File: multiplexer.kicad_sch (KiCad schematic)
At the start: 0 parts

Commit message: FINISH SCHEMATICS
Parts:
- added C6: 10uf, symbol Device:C
- added JP10, JP2, JP3, JP4, JP5: SolderJumper_2_Open, symbol Jumper:SolderJumper_2_Open
- added R10, R11, R12, R13, R14, R19: 10k, symbol Device:R
- added U2: TCA9548APWR, Package_SO:TSSOP-24_4.4x7.8mm_P0.65mm, symbol Interface_Expansion:TCA9548APWR
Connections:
- new net: JP10.2 (B), R10.2
- new net: JP5.2 (B), R14.2, U2.1 (A0)
- new net: JP4.2 (B), R13.2, U2.2 (A1)
- new net: JP2.2 (B), R19.2
- new net: JP3.1 (A), R12.2, U2.21 (A2)
- new net: R11.2, U2.3 (~{RESET})
- new net GND: C6.2, R12.1, R13.1, R14.1, U2.12 (GND)
- new net SC0: U2.5 (SC0)
- new net SC1: U2.7 (SC1)
- new net SC2: U2.9 (SC2)
- new net SC3: U2.11 (SC3)
- new net SC4: U2.14 (SC4)
- new net SC5: U2.16 (SC5)
- new net SC6: U2.18 (SC6)
- new net SC7: U2.20 (SC7)
- new net SCL_IN: JP10.1 (A), U2.22 (SCL)
- new net SD0: U2.4 (SD0)
- new net SD1: U2.6 (SD1)
- new net SD2: U2.8 (SD2)
- new net SD3: U2.10 (SD3)
- new net SD4: U2.13 (SD4)
- new net SD5: U2.15 (SD5)
- new net SD6: U2.17 (SD6)
- new net SD7: U2.19 (SD7)
- new net SDA_IN: JP2.1 (A), U2.23 (SDA)
- new net VCC: C6.1, JP3.2 (B), JP4.1 (A), JP5.1 (A), R10.1, R11.1, R19.1, U2.24 (VCC)

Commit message: assign footprints
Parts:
- C6: footprint (none) -> Capacitor_SMD:C_0201_0603Metric
- JP10: footprint (none) -> Jumper:SolderJumper-2_P1.3mm_Open_Pad1.0x1.5mm
- JP6: renamed from JP3; footprint (none) -> Jumper:SolderJumper-2_P1.3mm_Open_Pad1.0x1.5mm
- JP7: renamed from JP4; footprint (none) -> Jumper:SolderJumper-2_P1.3mm_Open_Pad1.0x1.5mm
- JP8: renamed from JP5; footprint (none) -> Jumper:SolderJumper-2_P1.3mm_Open_Pad1.0x1.5mm
- JP9: renamed from JP2; footprint (none) -> Jumper:SolderJumper-2_P1.3mm_Open_Pad1.0x1.5mm
- R15: renamed from R12; footprint (none) -> Resistor_SMD:R_0201_0603Metric
- R16: renamed from R13; footprint (none) -> Resistor_SMD:R_0201_0603Metric
- R17: renamed from R14; footprint (none) -> Resistor_SMD:R_0201_0603Metric
- R18: renamed from R11; footprint (none) -> Resistor_SMD:R_0201_0603Metric
- R19: footprint (none) -> Resistor_SMD:R_0201_0603Metric
- R20: renamed from R10; footprint (none) -> Resistor_SMD:R_0201_0603Metric
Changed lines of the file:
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@@
 			)
 		)
-		(property "Footprint" ""
+		(property "Footprint" "Jumper:SolderJumper-2_P1.3mm_Open_Pad1.0x1.5mm"
 			(at 125.73 63.5 0)
 			(effects
@@
 					(unit 1)
 				)
+				(path "/3c2fce68-ba60-4bda-a294-ddd60ff77106/3c684fcd-f9b8-4f06-8c65-1f616a3a4c49"
+					(reference "JP1")
+					(unit 1)
+				)
 			)
 		)
@@
 		(dnp no)
 		(fields_autoplaced yes)
-		(property "Reference" "#PWR024"
+		(property "Reference" "#PWR038"
 			(at 109.22 77.47 0)
 			(effects
@@
 					(unit 1)
 				)
+				(path "/3c2fce68-ba60-4bda-a294-ddd60ff77106/3c684fcd-f9b8-4f06-8c65-1f616a3a4c49"
+					(reference "#PWR080")
+					(unit 1)
+				)
 			)
 		)
@@
 		(on_board yes)
 		(dnp no)
-		(property "Reference" "JP5"
+		(property "Reference" "JP8"
 			(at 113.03 109.22 90)
 			(effects
@@
 			)
 		)
-		(property "Footprint" ""
+		(property "Footprint" "Jumper:SolderJumper-2_P1.3mm_Open_Pad1.0x1.5mm"
 			(at 111.76 107.95 0)
 			(effects
@@
 		(dnp no)
 		(fields_autoplaced yes)
-		(property "Reference" "#PWR031"
+		(property "Reference" "#PWR018"
 			(at 88.9 99.06 0)
 			(effects
@@
 		(on_board yes)
 		(dnp no)
-		(property "Reference" "JP4"
+		(property "Reference" "JP7"
 			(at 102.108 105.41 90)
 			(effects
@@
 			)
 		)
-		(property "Footprint" ""
+		(property "Footprint" "Jumper:SolderJumper-2_P1.3mm_Open_Pad1.0x1.5mm"
 			(at 106.68 105.41 0)
 			(effects
@@
 		(dnp no)
 		(fields_autoplaced yes)
-		(property "Reference" "#PWR032"
+		(property "Reference" "#PWR019"
 			(at 88.9 101.6 0)
 			(effects
@@
 		(dnp no)
 		(fields_autoplaced yes)
-		(property "Reference" "#PWR036"
+		(property "Reference" "#PWR039"
 			(at 111.76 107.95 0)
 			(effects
@@
 		(on_board yes)
 		(dnp no)
-		(property "Reference" "JP2"
+		(property "Reference" "JP9"
 			(at 113.792 62.23 90)
 			(effects
@@
 			)
 		)
-		(property "Footprint" ""
+		(property "Footprint" "Jumper:SolderJumper-2_P1.3mm_Open_Pad1.0x1.5mm"
 			(at 119.38 63.5 0)
 			(effects
@@
 					(unit 1)
 				)
+				(path "/3c2fce68-ba60-4bda-a294-ddd60ff77106/3c684fcd-f9b8-4f06-8c65-1f616a3a4c49"
+					(reference "#PWR079")
+					(unit 1)
+				)
 			)
 		)
@@
 		(dnp no)
 		(fields_autoplaced yes)
-		(property "Reference" "#PWR034"
+		(property "Reference" "#PWR021"
 			(at 104.14 95.25 0)
 			(effects
@@
 		(dnp no)
 		(fields_autoplaced yes)
-		(property "Reference" "#PWR029"
+		(property "Reference" "#PWR044"
 			(at 175.26 52.07 0)
 			(effects
@@
 		(on_board yes)
 		(dnp no)
-		(property "Reference" "JP3"
+		(property "Reference" "JP6"
 			(at 105.41 95.504 90)
 			(effects
@@
 			)
 		)
-		(property "Footprint" ""
+		(property "Footprint" "Jumper:SolderJumper-2_P1.3mm_Open_Pad1.0x1.5mm"
 			(at 104.14 95.25 0)
 			(effects
@@
 		(on_board yes)
 		(dnp no)
-		(property "Reference" "R13"
+		(property "Reference" "R16"
 			(at 97.536 107.696 0)
 			(effects
@@
 			)
 		)
-		(property "Footprint" ""
+		(property "Footprint" "Resistor_SMD:R_0201_0603Metric"
 			(at 99.06 103.378 90)
 			(effects
@@
 		(dnp no)
 		(fields_autoplaced yes)
-		(property "Reference" "#PWR030"
+		(property "Reference" "#PWR045"
 			(at 175.26 63.5 0)
 			(effects
@@
 					(unit 1)
 				)
+				(path "/3c2fce68-ba60-4bda-a294-ddd60ff77106/3c684fcd-f9b8-4f06-8c65-1f616a3a4c49"
+					(reference "U1")
+					(unit 1)
+				)
 			)
 		)
@@
 		(on_board yes)
 		(dnp no)
-		(property "Reference" "R11"
+		(property "Reference" "R18"
 			(at 103.124 75.946 0)
 			(effects
@@
 			)
 		)
-		(property "Footprint" ""
+		(property "Footprint" "Resistor_SMD:R_0201_0603Metric"
 			(at 107.442 77.47 90)
 			(effects
@@
 		(dnp no)
 		(fields_autoplaced yes)
-		(property "Reference" "R10"
+		(property "Reference" "R20"
 			(at 128.27 54.6099 0)
 			(effects
@@
 			)
 		)
-		(property "Footprint" ""
+		(property "Footprint" "Resistor_SMD:R_0201_0603Metric"
 			(at 123.952 55.88 90)
 			(effects
@@
 			)
 		)
-		(property "Footprint" ""
+		(property "Footprint" "Capacitor_SMD:C_0201_0603Metric"
 			(at 124.1552 119.38 0)
 			(effects
@@
 					(unit 1)
 				)
+				(path "/3c2fce68-ba60-4bda-a294-ddd60ff77106/3c684fcd-f9b8-4f06-8c65-1f616a3a4c49"
+					(reference "C5")
+					(unit 1)
+				)
 			)
 		)
@@
 		(on_board yes)
 		(dnp no)
-		(property "Reference" "R14"
+		(property "Reference" "R17"
 			(at 97.536 110.236 0)
 			(effects
@@
 			)
 		)
-		(property "Footprint" ""
+		(property "Footprint" "Resistor_SMD:R_0201_0603Metric"
 			(at 99.06 105.918 90)
 			(effects
@@
 		(dnp no)
 		(fields_autoplaced yes)
-		(property "Reference" "#PWR023"
+		(property "Reference" "#PWR043"
 			(at 125.73 55.88 0)
 			(effects
@@
 		(on_board yes)
 		(dnp no)
-		(property "Reference" "R12"
+		(property "Reference" "R15"
 			(at 97.536 105.156 0)
 			(effects
@@
 			)
 		)
-		(property "Footprint" ""
+		(property "Footprint" "Resistor_SMD:R_0201_0603Metric"
 			(at 99.06 100.838 90)
 			(effects
@@
 					(unit 1)
 				)
+				(path "/3c2fce68-ba60-4bda-a294-ddd60ff77106/3c684fcd-f9b8-4f06-8c65-1f616a3a4c49"
+					(reference "#PWR081")
+					(unit 1)
+				)
 			)
 		)
@@
 		(dnp no)
 		(fields_autoplaced yes)
-		(property "Reference" "#PWR033"
+		(property "Reference" "#PWR020"
 			(at 88.9 104.14 0)
 			(effects
@@
 			)
 		)
-		(property "Footprint" ""
+		(property "Footprint" "Resistor_SMD:R_0201_0603Metric"
 			(at 117.602 55.88 90)
 			(effects
@@
 					(unit 1)
 				)
+				(path "/3c2fce68-ba60-4bda-a294-ddd60ff77106/3c684fcd-f9b8-4f06-8c65-1f616a3a4c49"
+					(reference "R9")
+					(unit 1)
+				)
 			)
 		)
@@
 		(dnp no)
 		(fields_autoplaced yes)
-		(property "Reference" "#PWR035"
+		(property "Reference" "#PWR037"
 			(at 106.68 105.41 0)
 			(effects

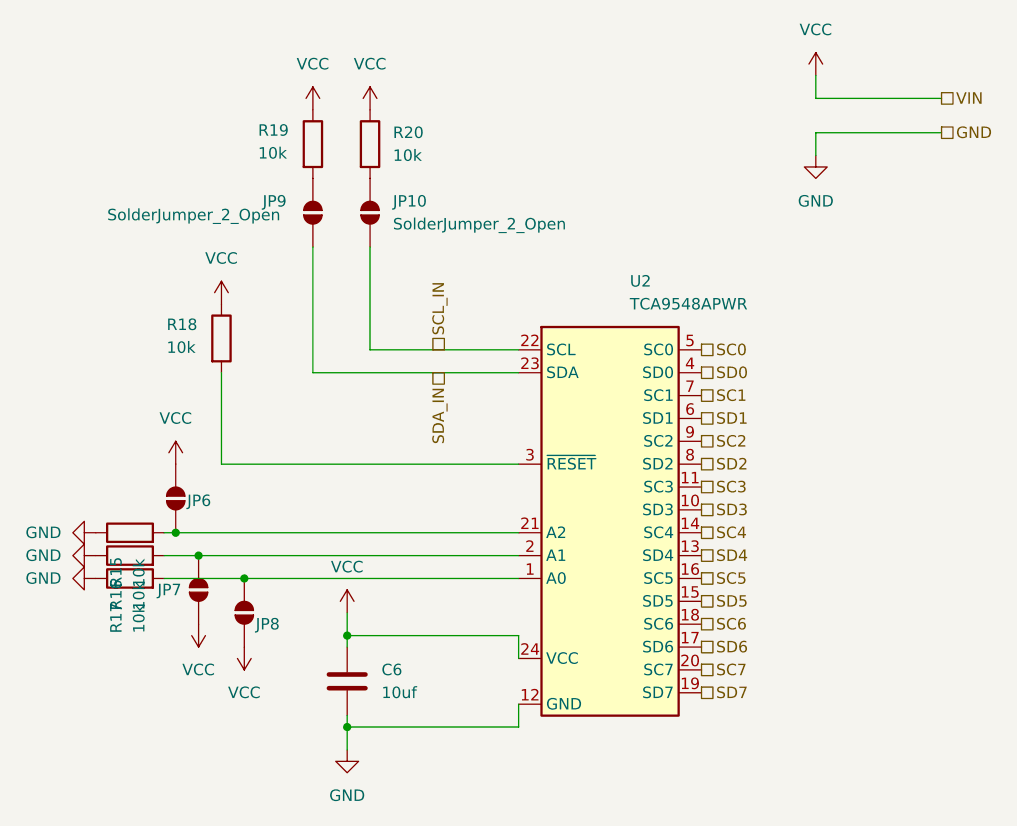
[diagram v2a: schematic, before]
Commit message: Add new lipo charger to pcb
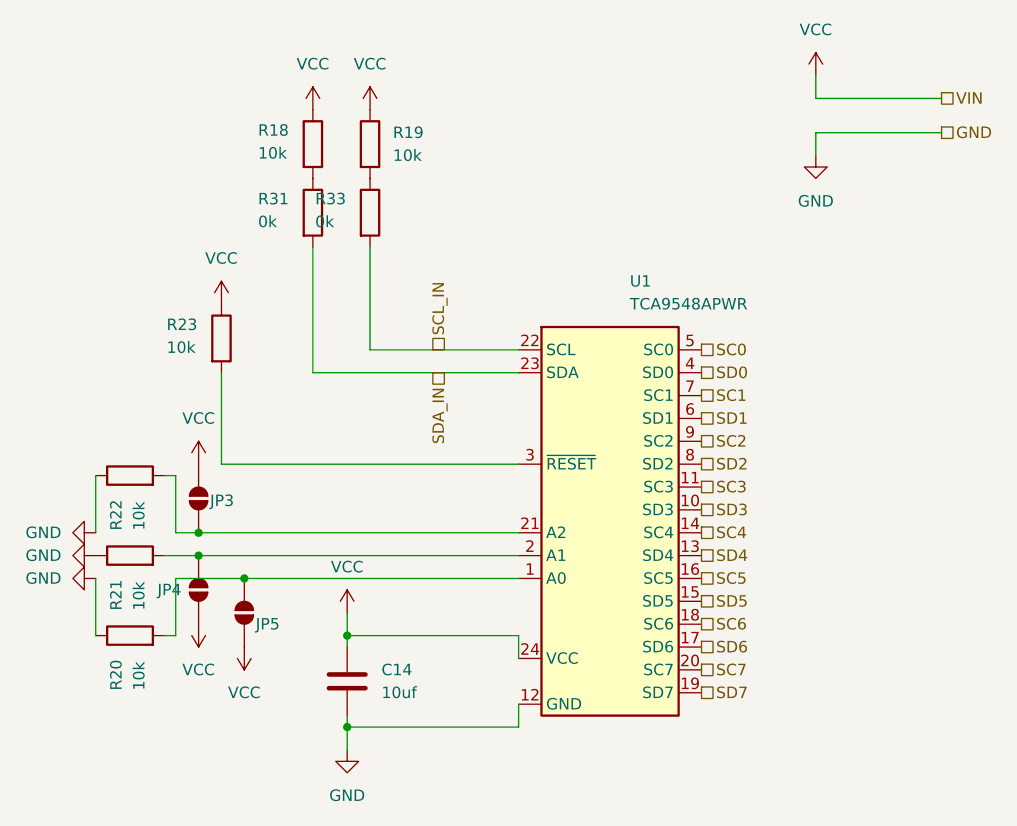
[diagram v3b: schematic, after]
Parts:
- removed JP10, JP9: SolderJumper_2_Open, Jumper:SolderJumper-2_P1.3mm_Open_Pad1.0x1.5mm, symbol Jumper:SolderJumper_2_Open
- added R31, R33: 0k, Resistor_SMD:R_0201_0603Metric, symbol Device:R
- renumbered C6 to C14, JP6 to JP3, JP7 to JP4, JP8 to JP5, R19 to R18, R20 to R19, R17 to R20, R16 to R21, R15 to R22, R18 to R23, U2 to U1
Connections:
- net SCL_IN: now also R33.2
- net SDA_IN: now also R31.2
- net at R19.2: now also R33.1
- net at R18.2: now also R31.1
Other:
- moved on the sheet: JP3, R20, R22

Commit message: a lot of work on pcb
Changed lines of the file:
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@@
+		)
+	)
+	(hierarchical_label "VIN"
+		(shape passive)
+		(at 125.73 52.07 90)
+		(fields_autoplaced yes)
+		(effects
+			(font
+				(size 1.27 1.27)
+			)
+			(justify left)
 		)
 	)
@@
 		)
 	)
+	(hierarchical_label "VIN"
+		(shape passive)
+		(at 119.38 52.07 90)
+		(fields_autoplaced yes)
+		(effects
+			(font
+				(size 1.27 1.27)
+			)
+			(justify left)
+		)
+	)
 	(hierarchical_label "SC6"
 		(shape passive)
@@
 		)
 	)
+	(hierarchical_label "VIN"
+		(shape passive)
+		(at 109.22 73.66 90)
+		(fields_autoplaced yes)
+		(effects
+			(font
+				(size 1.27 1.27)
+			)
+			(justify left)
+		)
+	)
 	(hierarchical_label "SC1"
 		(shape passive)
@@
 			)
 			(justify left)
-		)
-	)
-	(symbol
-		(lib_id "power:VCC")
-		(at 109.22 73.66 0)
-		(unit 1)
-		(exclude_from_sim no)
-		(in_bom yes)
-		(on_board yes)
-		(dnp no)
-		(fields_autoplaced yes)
-		(property "Reference" "#PWR024"
-			(at 109.22 77.47 0)
-			(effects
-				(font
-					(size 1.27 1.27)
-				)
-				(hide yes)
-			)
-		)
-		(property "Value" "VCC"
-			(at 109.22 68.58 0)
-			(effects
-				(font
-					(size 1.27 1.27)
-				)
-			)
-		)
-		(property "Footprint" ""
-			(at 109.22 73.66 0)
-			(effects
-				(font
-					(size 1.27 1.27)
-				)
-				(hide yes)
-			)
-		)
-		(property "Datasheet" ""
-			(at 109.22 73.66 0)
-			(effects
-				(font
-					(size 1.27 1.27)
-				)
-				(hide yes)
-			)
-		)
-		(property "Description" "Power symbol creates a global label with name \"VCC\""
-			(at 109.22 73.66 0)
-			(effects
-				(font
-					(size 1.27 1.27)
-				)
-				(hide yes)
-			)
-		)
-		(pin "1"
-		)
-		(instances
-			(project "shadow"
-				(path "/3c2fce68-ba60-4bda-a294-ddd60ff77106/3c684fcd-f9b8-4f06-8c65-1f616a3a4c49"
-					(reference "#PWR024")
-					(unit 1)
-				)
-				(path "/3c2fce68-ba60-4bda-a294-ddd60ff77106/5f8222d1-2a00-4590-a900-2f925c082a60"
-					(reference "#PWR021")
-					(unit 1)
-				)
-			)
 		)
 	)
@@
 	(symbol
 		(lib_id "power:VCC")
-		(at 119.38 52.07 0)
-		(unit 1)
-		(exclude_from_sim no)
-		(in_bom yes)
-		(on_board yes)
-		(dnp no)
-		(fields_autoplaced yes)
-		(property "Reference" "#PWR079"
-			(at 119.38 55.88 0)
-			(effects
-				(font
-					(size 1.27 1.27)
-				)
-				(hide yes)
-			)
-		)
-		(property "Value" "VCC"
-			(at 119.38 46.99 0)
-			(effects
-				(font
-					(size 1.27 1.27)
-				)
-			)
-		)
-		(property "Footprint" ""
-			(at 119.38 52.07 0)
-			(effects
-				(font
-					(size 1.27 1.27)
-				)
-				(hide yes)
-			)
-		)
-		(property "Datasheet" ""
-			(at 119.38 52.07 0)
-			(effects
-				(font
-					(size 1.27 1.27)
-				)
-				(hide yes)
-			)
-		)
-		(property "Description" "Power symbol creates a global label with name \"VCC\""
-			(at 119.38 52.07 0)
-			(effects
-				(font
-					(size 1.27 1.27)
-				)
-				(hide yes)
-			)
-		)
-		(pin "1"
-		)
-		(instances
-			(project "shadow"
-				(path "/3c2fce68-ba60-4bda-a294-ddd60ff77106/3c684fcd-f9b8-4f06-8c65-1f616a3a4c49"
-					(reference "#PWR079")
-					(unit 1)
-				)
-				(path "/3c2fce68-ba60-4bda-a294-ddd60ff77106/5f8222d1-2a00-4590-a900-2f925c082a60"
-					(reference "#PWR038")
-					(unit 1)
-				)
-			)
-		)
-	)
-	(symbol
-		(lib_id "power:VCC")
 		(at 106.68 91.44 0)
 		(unit 1)
@@
 	)
 	(symbol
-		(lib_id "power:VCC")
-		(at 125.73 52.07 0)
-		(unit 1)
-		(exclude_from_sim no)
-		(in_bom yes)
-		(on_board yes)
-		(dnp no)
-		(fields_autoplaced yes)
-		(property "Reference" "#PWR023"
-			(at 125.73 55.88 0)
-			(effects
-				(font
-					(size 1.27 1.27)
-				)
-				(hide yes)
-			)
-		)
-		(property "Value" "VCC"
-			(at 125.73 46.99 0)
-			(effects
-				(font
-					(size 1.27 1.27)
-				)
-			)
-		)
-		(property "Footprint" ""
-			(at 125.73 52.07 0)
-			(effects
-				(font
-					(size 1.27 1.27)
-				)
-				(hide yes)
-			)
-		)
-		(property "Datasheet" ""
-			(at 125.73 52.07 0)
-			(effects
-				(font
-					(size 1.27 1.27)
-				)
-				(hide yes)
-			)
-		)
-		(property "Description" "Power symbol creates a global label with name \"VCC\""
-			(at 125.73 52.07 0)
-			(effects
-				(font
-					(size 1.27 1.27)
-				)
-				(hide yes)
-			)
-		)
-		(pin "1"
-		)
-		(instances
-			(project "shadow"
-				(path "/3c2fce68-ba60-4bda-a294-ddd60ff77106/3c684fcd-f9b8-4f06-8c65-1f616a3a4c49"
-					(reference "#PWR023")
-					(unit 1)
-				)
-				(path "/3c2fce68-ba60-4bda-a294-ddd60ff77106/5f8222d1-2a00-4590-a900-2f925c082a60"
-					(reference "#PWR041")
-					(unit 1)
-				)
-			)
-		)
-	)
-	(symbol
 		(lib_id "Device:R")
 		(at 99.06 92.71 90)
@@
 		(dnp no)
 		(property "Reference" "R33"
-			(at 119.634 61.976 0)
+			(at 128.524 61.976 0)
 			(effects
 				(font
@@
 		)
 		(property "Value" "0k"
-			(at 119.634 64.516 0)
-			(effects
-				(font
+			(at 128.524 64.516 0)
+			(effects
+				(font

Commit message: finish pcb
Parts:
- C14: footprint Capacitor_SMD:C_0201_0603Metric -> Capacitor_SMD:C_1206_3216Metric
- R18, R19, R20, R21, R22, R23, R31, R33: footprint Resistor_SMD:R_0201_0603Metric -> Resistor_SMD:R_1206_3216Metric
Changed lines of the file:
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@@
 			)
 		)
-		(property "Footprint" "Resistor_SMD:R_0201_0603Metric"
+		(property "Footprint" "Resistor_SMD:R_1206_3216Metric"
 			(at 99.06 103.378 90)
 			(effects
@@
 			)
 		)
-		(property "Footprint" "Resistor_SMD:R_0201_0603Metric"
+		(property "Footprint" "Resistor_SMD:R_1206_3216Metric"
 			(at 107.442 77.47 90)
 			(effects
@@
 			)
 		)
-		(property "Footprint" "Resistor_SMD:R_0201_0603Metric"
+		(property "Footprint" "Resistor_SMD:R_1206_3216Metric"
 			(at 123.952 55.88 90)
 			(effects
@@
 			)
 		)
-		(property "Footprint" "Capacitor_SMD:C_0201_0603Metric"
+		(property "Footprint" "Capacitor_SMD:C_1206_3216Metric"
 			(at 124.1552 119.38 0)
 			(effects
@@
 			)
 		)
-		(property "Footprint" "Resistor_SMD:R_0201_0603Metric"
+		(property "Footprint" "Resistor_SMD:R_1206_3216Metric"
 			(at 99.06 112.268 90)
 			(effects
@@
 			)
 		)
-		(property "Footprint" "Resistor_SMD:R_0201_0603Metric"
+		(property "Footprint" "Resistor_SMD:R_1206_3216Metric"
 			(at 117.602 63.5 90)
 			(effects
@@
 			)
 		)
-		(property "Footprint" "Resistor_SMD:R_0201_0603Metric"
+		(property "Footprint" "Resistor_SMD:R_1206_3216Metric"
 			(at 99.06 94.488 90)
 			(effects
@@
 			)
 		)
-		(property "Footprint" "Resistor_SMD:R_0201_0603Metric"
+		(property "Footprint" "Resistor_SMD:R_1206_3216Metric"
 			(at 117.602 55.88 90)
 			(effects
@@
 			)
 		)
-		(property "Footprint" "Resistor_SMD:R_0201_0603Metric"
+		(property "Footprint" "Resistor_SMD:R_1206_3216Metric"
 			(at 123.952 63.5 90)
 			(effects
